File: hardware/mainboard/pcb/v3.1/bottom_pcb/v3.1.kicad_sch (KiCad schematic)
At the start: 8 parts, among them J1 Conn_01x03_Male, J2 Conn_01x03_Male, U1 ATtiny1626, U2 ATtiny1626

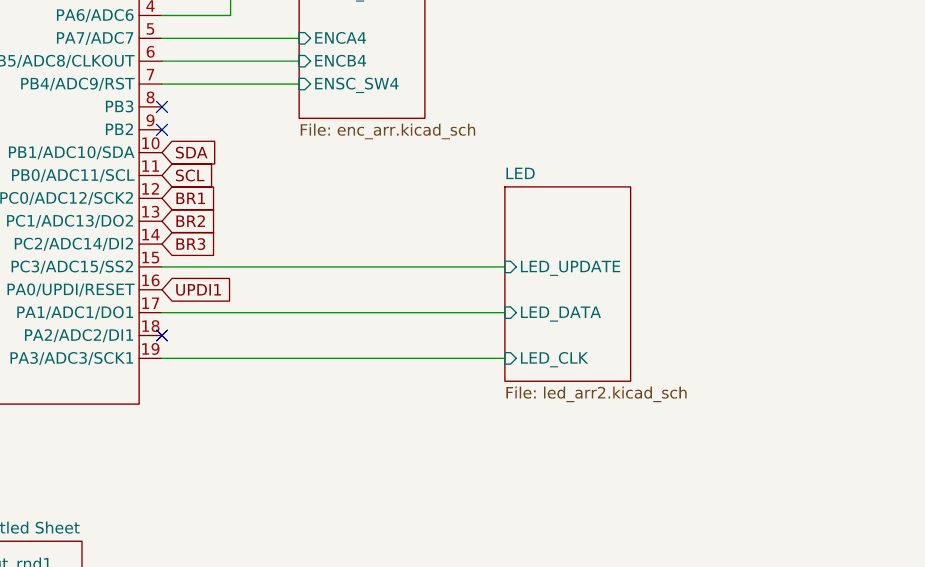
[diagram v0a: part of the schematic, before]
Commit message: pcb cut off
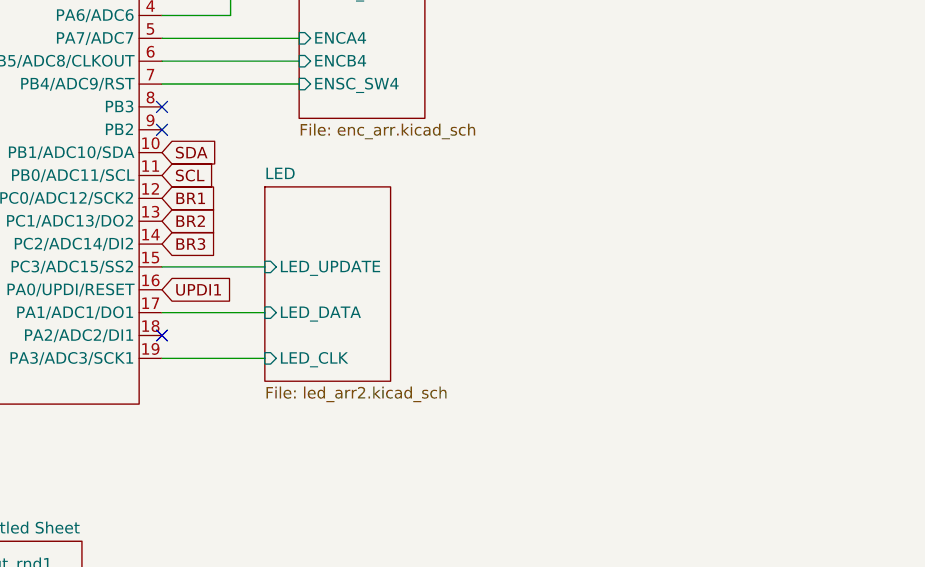
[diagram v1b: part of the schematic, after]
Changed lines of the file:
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@@
     (stroke (width 0) (type default))
   )
-  (wire (pts (xy 53.34 80.01) (xy 91.44 80.01))
-    (stroke (width 0) (type default))
-  )
-  (wire (pts (xy 53.34 74.93) (xy 91.44 74.93))
+  (wire (pts (xy 53.34 80.01) (xy 64.77 80.01))
+    (stroke (width 0) (type default))
+  )
+  (wire (pts (xy 53.34 74.93) (xy 64.77 74.93))
     (stroke (width 0) (type default))
   )
@@
     (stroke (width 0) (type default))
   )
-  (wire (pts (xy 53.34 85.09) (xy 91.44 85.09))
+  (wire (pts (xy 53.34 85.09) (xy 64.77 85.09))
     (stroke (width 0) (type default))
   )
@@
     )
   )
-  (symbol (lib_name "ATtiny1626_1") (lib_id "3dAudioSym:ATtiny1626") (at 191.77 82.55 0) (unit 1)
+  (symbol (lib_id "3dAudioSym:ATtiny1626") (at 191.77 82.55 0) (unit 1)
     (in_bom yes) (on_board yes) (dnp no) (fields_autoplaced)
     (property "Reference" "U2" (at 179.07 80.0099 0)
@@
     )
   )
-  (sheet (at 91.44 66.04) (size 13.97 21.59) (fields_autoplaced)
+  (sheet (at 64.77 66.04) (size 13.97 21.59) (fields_autoplaced)
     (stroke (width 0.1524) (type solid))
     (fill (color 0 0 0 0.0000))
-    (property "Sheetname" "LED" (at 91.44 65.3284 0)
+    (property "Sheetname" "LED" (at 64.77 65.3284 0)
       (effects (font (size 1.27 1.27)) (justify left bottom))
     )
-    (property "Sheetfile" "led_arr2.kicad_sch" (at 91.44 88.2146 0)
+    (property "Sheetfile" "led_arr2.kicad_sch" (at 64.77 88.2146 0)
       (effects (font (size 1.27 1.27)) (justify left top))
     )
-    (pin "LED_CLK" input (at 91.44 85.09 180)
-      (effects (font (size 1.27 1.27)) (justify left))
-    )
-    (pin "LED_DATA" input (at 91.44 80.01 180)
-      (effects (font (size 1.27 1.27)) (justify left))
-    )
-    (pin "LED_UPDATE" input (at 91.44 74.93 180)
-      (effects (font (size 1.27 1.27)) (justify left))
-    )
+    (pin "LED_CLK" input (at 64.77 85.09 180)
+      (effects (font (size 1.27 1.27)) (justify left))
+    )
+    (pin "LED_DATA" input (at 64.77 80.01 180)
+      (effects (font (size 1.27 1.27)) (justify left))
+    )
+    (pin "LED_UPDATE" input (at 64.77 74.93 180)
+      (effects (font (size 1.27 1.27)) (justify left))
+    )
